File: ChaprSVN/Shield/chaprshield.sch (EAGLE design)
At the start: 2 parts

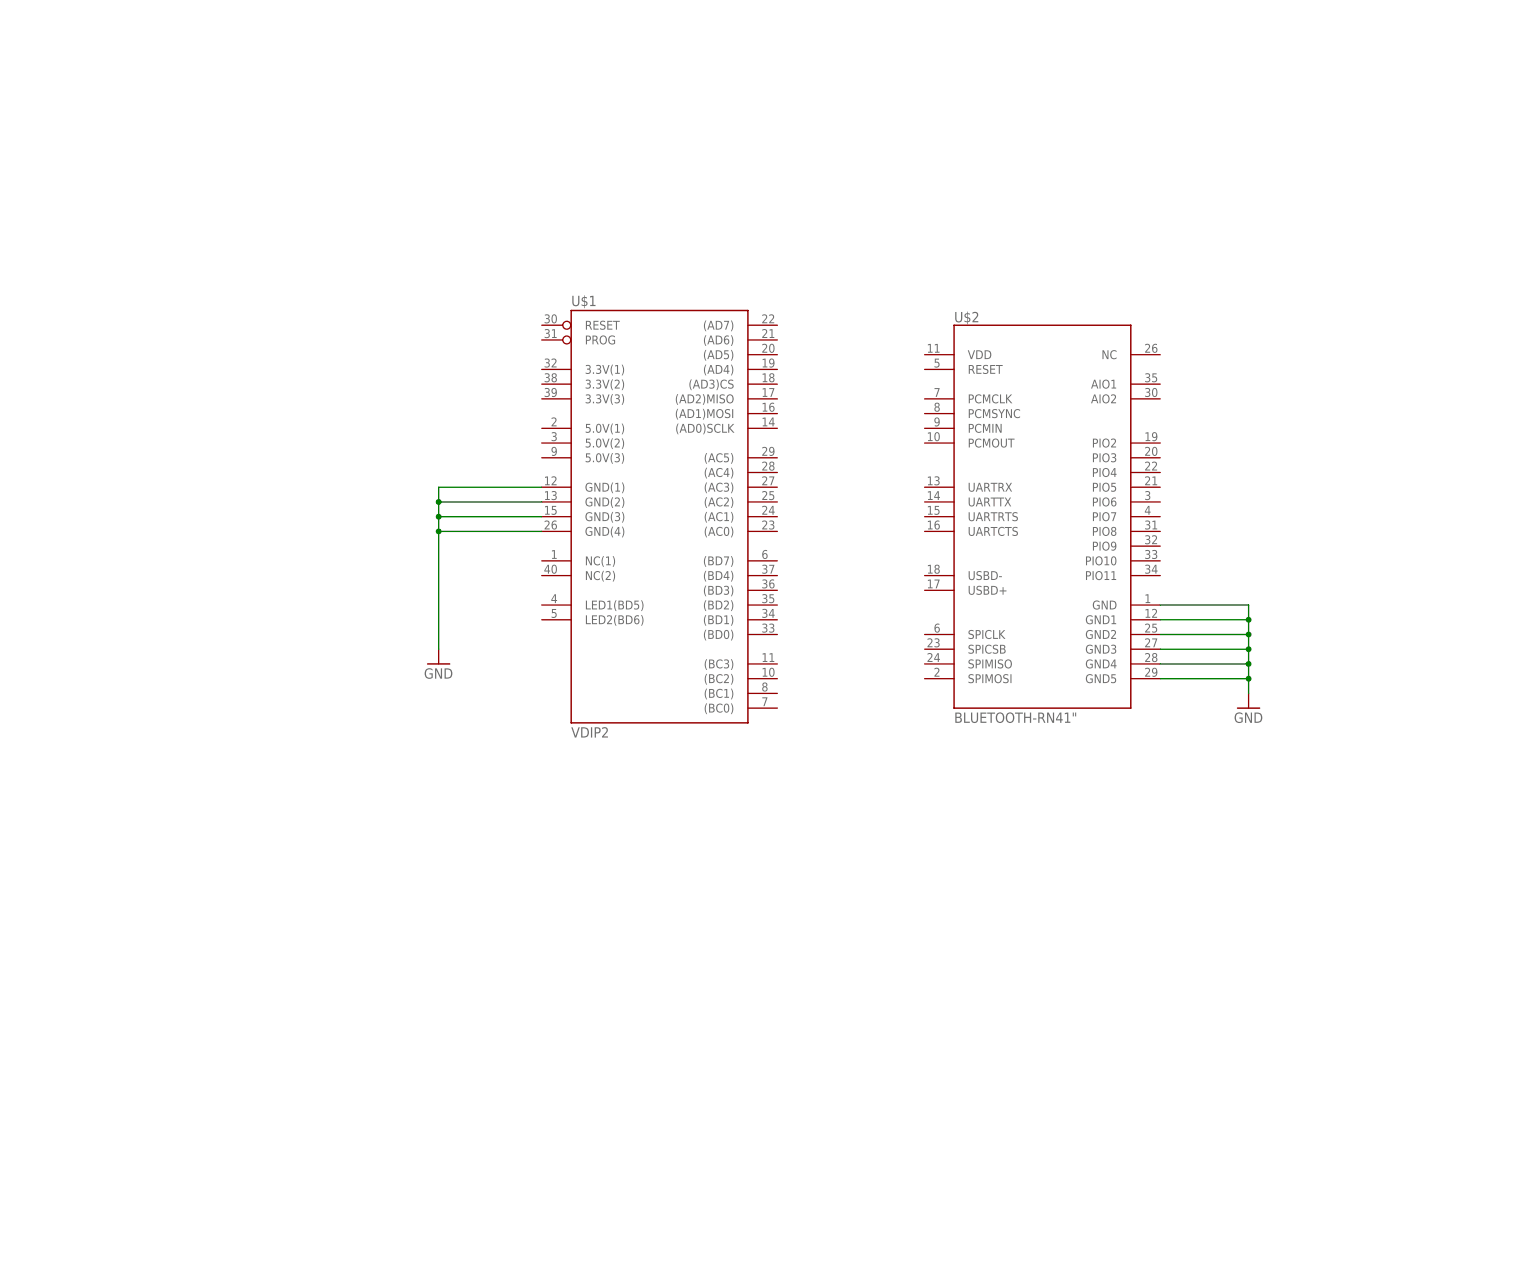
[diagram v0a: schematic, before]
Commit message: Added pin headers and started wiring.
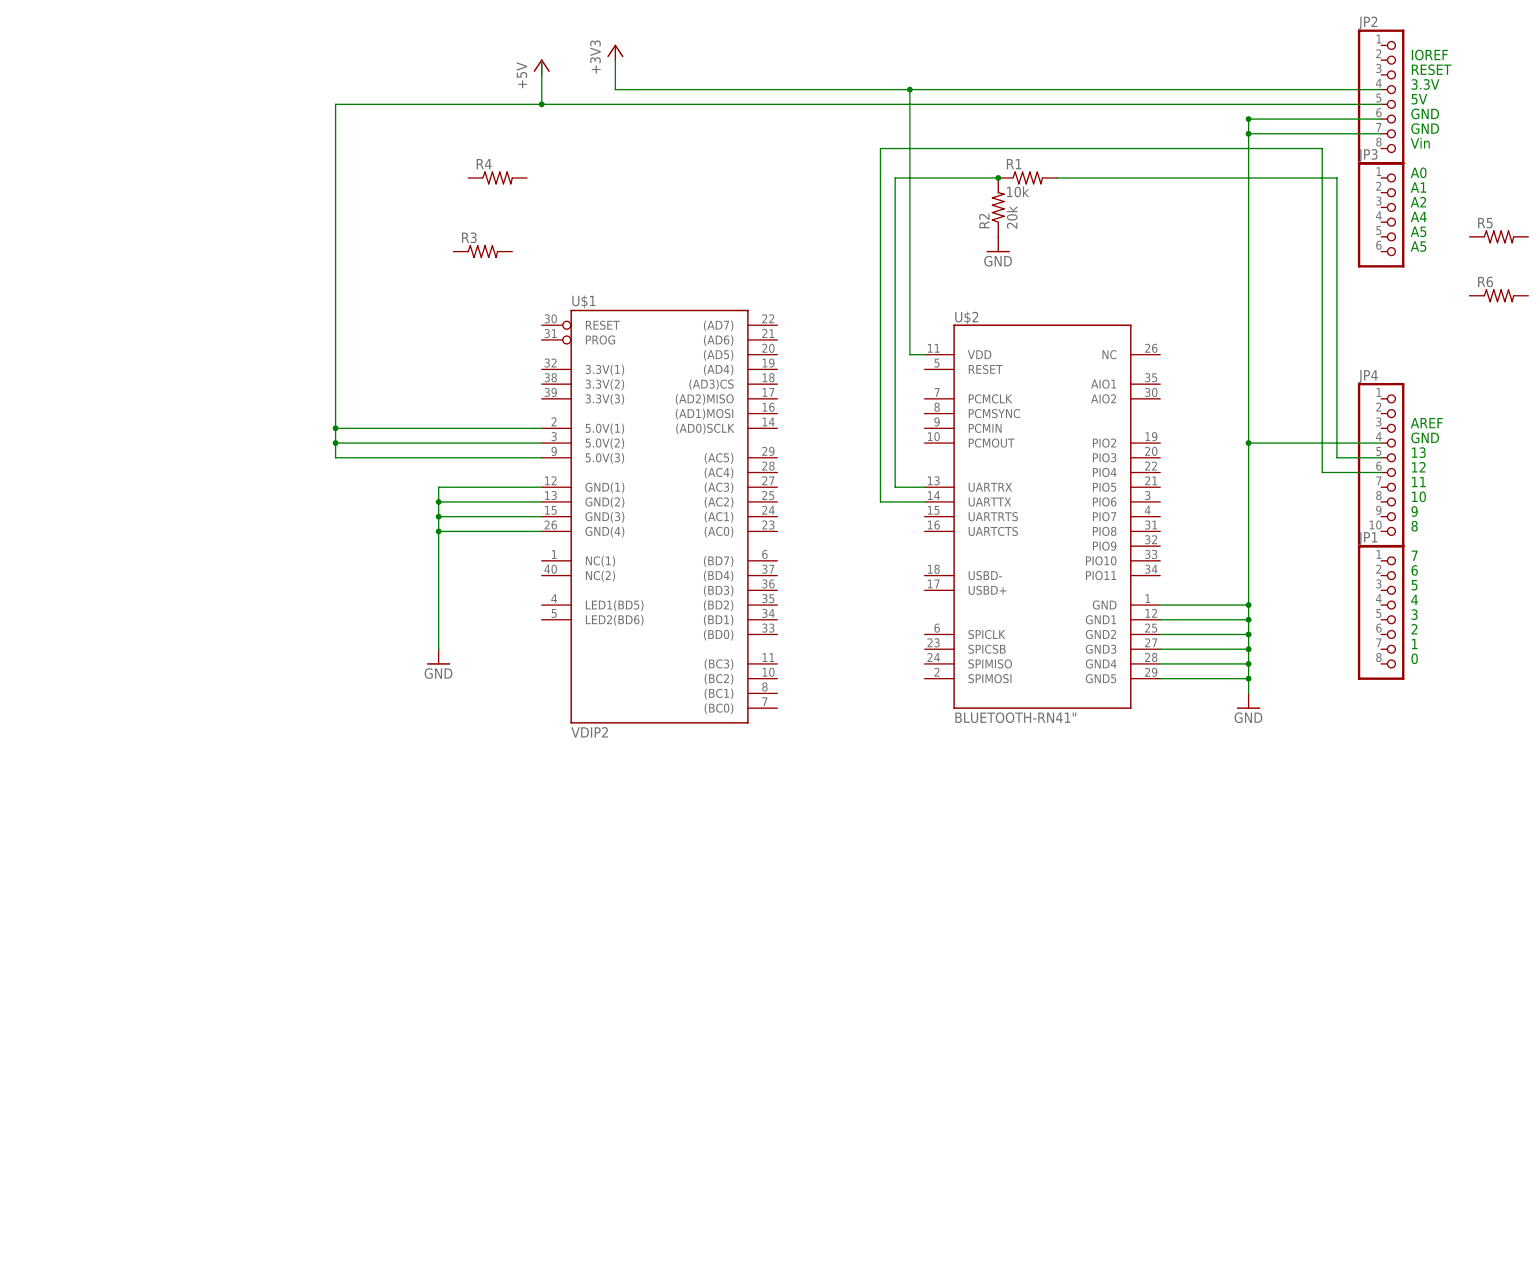
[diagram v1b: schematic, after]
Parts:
- added JP1, JP2: (no value), pinhead:PINHD-1X8
- added JP3: (no value), pinhead:PINHD-1X6
- added JP4: (no value), pinhead:PINHD-1X10
- added R1: 10k, resistor:R-US_0207/10
- added R2: 20k, resistor:R-US_0207/10
- added R3, R4, R5, R6: (no value), resistor:R-US_0207/10
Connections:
- new net N$1: JP2.5, U$1.5.0V(1), U$1.5.0V(2), U$1.5.0V(3)
- new net N$2: JP2.4, U$2.VDD
- new net N$3: JP4.5, R1.2
- new net N$4: R1.1, R2.2, U$2.UARTRX
- new net N$5: JP4.6, U$2.UARTTX
- net GND: now also JP2.6, JP2.7, JP4.4, R2.1
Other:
- note added: "0"
- note added: "1"
- note added: "10"
- note added: "11"
- note added: "12"
- note added: "13"
- note added: "2"
- note added: "3"
- note added: "3.3V"
- note added: "4"
- note added: "5"
- note added: "5V"
- note added: "6"
- note added: "7"
- note added: "8"
- note added: "9"
- note added: "A0"
- note added: "A1"
- note added: "A2"
- note added: "A4"
- note added: "A5"
- note added: "AREF"
- note added: "GND"
- note added: "IOREF"
- note added: "RESET"
- note added: "Vin"
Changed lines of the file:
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@@
 <part name="U$2" library="SparkFun-RF" deviceset="BLUETOOTH-RN41" device="&quot;"/>
 <part name="GND2" library="supply1" deviceset="GND" device=""/>
+<part name="JP1" library="pinhead" deviceset="PINHD-1X8" device=""/>
+<part name="JP2" library="pinhead" deviceset="PINHD-1X8" device=""/>
+<part name="JP3" library="pinhead" deviceset="PINHD-1X6" device=""/>
+<part name="JP4" library="pinhead" deviceset="PINHD-1X10" device=""/>
+<part name="+3V1" library="supply1" deviceset="+3V3" device=""/>
+<part name="P+1" library="supply1" deviceset="+5V" device=""/>
+<part name="R1" library="resistor" deviceset="R-US_" device="0207/10" value="10k"/>
+<part name="R2" library="resistor" deviceset="R-US_" device="0207/10" value="20k"/>
+<part name="R3" library="resistor" deviceset="R-US_" device="0207/10"/>
+<part name="R4" library="resistor" deviceset="R-US_" device="0207/10"/>
+<part name="R5" library="resistor" deviceset="R-US_" device="0207/10"/>
+<part name="R6" library="resistor" deviceset="R-US_" device="0207/10"/>
+<part name="GND3" library="supply1" deviceset="GND" device=""/>
 </parts>
 <sheets>
 <sheet>
 <plain>
+<text x="154.94" y="60.96" size="1.778" layer="91">13</text>
+<text x="154.94" y="58.42" size="1.778" layer="91">12</text>
+<text x="154.94" y="55.88" size="1.778" layer="91">11</text>
+<text x="154.94" y="53.34" size="1.778" layer="91">10</text>
+<text x="154.94" y="50.8" size="1.778" layer="91">9</text>
+<text x="154.94" y="48.26" size="1.778" layer="91">8</text>
+<text x="154.94" y="43.18" size="1.778" layer="91">7</text>
+<text x="154.94" y="40.64" size="1.778" layer="91">6</text>
+<text x="154.94" y="38.1" size="1.778" layer="91">5</text>
+<text x="154.94" y="35.56" size="1.778" layer="91">4</text>
+<text x="154.94" y="33.02" size="1.778" layer="91">3</text>
+<text x="154.94" y="30.48" size="1.778" layer="91">2</text>
+<text x="154.94" y="27.94" size="1.778" layer="91">1</text>
+<text x="154.94" y="25.4" size="1.778" layer="91">0</text>
+<text x="154.94" y="63.5" size="1.778" layer="91">GND</text>
+<text x="154.94" y="116.84" size="1.778" layer="91">GND</text>
+<text x="154.94" y="119.38" size="1.778" layer="91">GND</text>
+<text x="154.94" y="96.52" size="1.778" layer="91">A5</text>
+<text x="154.94" y="99.06" size="1.778" layer="91">A5</text>
+<text x="154.94" y="101.6" size="1.778" layer="91">A4</text>
+<text x="154.94" y="104.14" size="1.778" layer="91">A2</text>
+<text x="154.94" y="106.68" size="1.778" layer="91">A1</text>
+<text x="154.94" y="109.22" size="1.778" layer="91">A0</text>
+<text x="154.94" y="114.3" size="1.778" layer="91">Vin</text>
+<text x="154.94" y="121.92" size="1.778" layer="91">5V</text>
+<text x="154.94" y="124.46" size="1.778" layer="91">3.3V</text>
+<text x="154.94" y="127" size="1.778" layer="91">RESET</text>
+<text x="154.94" y="129.54" size="1.778" layer="91">IOREF</text>
+<text x="154.94" y="66.04" size="1.778" layer="91">AREF</text>
 </plain>
 <instances>
@@
 <instance part="U$2" gate="G$1" x="91.44" y="50.8"/>
 <instance part="GND2" gate="1" x="127" y="17.78"/>
+<instance part="JP1" gate="A" x="152.4" y="33.02"/>
+<instance part="JP2" gate="A" x="152.4" y="121.92"/>
+<instance part="JP3" gate="A" x="152.4" y="101.6"/>
+<instance part="JP4" gate="A" x="152.4" y="60.96"/>
+<instance part="+3V1" gate="G$1" x="17.78" y="132.08"/>
+<instance part="P+1" gate="1" x="5.08" y="129.54"/>
+<instance part="R1" gate="G$1" x="88.9" y="109.22"/>
+<instance part="R2" gate="G$1" x="83.82" y="104.14" rot="R90"/>
+<instance part="R3" gate="G$1" x="-5.08" y="96.52"/>
+<instance part="R4" gate="G$1" x="-2.54" y="109.22"/>
+<instance part="R5" gate="G$1" x="170.18" y="99.06"/>
+<instance part="R6" gate="G$1" x="170.18" y="88.9"/>
+<instance part="GND3" gate="1" x="83.82" y="96.52"/>
 </instances>
 <busses>
@@
 <junction x="127" y="25.4"/>
 <junction x="127" y="22.86"/>
+<wire x1="127" y1="63.5" x2="127" y2="35.56" width="0.1524" layer="91"/>
+<junction x="127" y="35.56"/>
+<pinref part="JP4" gate="A" pin="4"/>
+<wire x1="149.86" y1="63.5" x2="127" y2="63.5" width="0.1524" layer="91"/>
+<pinref part="JP2" gate="A" pin="6"/>
+<wire x1="149.86" y1="119.38" x2="127" y2="119.38" width="0.1524" layer="91"/>
+<wire x1="127" y1="119.38" x2="127" y2="116.84" width="0.1524" layer="91"/>
+<pinref part="JP2" gate="A" pin="7"/>
+<wire x1="127" y1="116.84" x2="127" y2="63.5" width="0.1524" layer="91"/>
+<wire x1="149.86" y1="116.84" x2="127" y2="116.84" width="0.1524" layer="91"/>
+<junction x="127" y="119.38"/>
+<junction x="127" y="116.84"/>
+<junction x="127" y="63.5"/>
+</segment>
+<segment>
+<pinref part="R2" gate="G$1" pin="1"/>
+<pinref part="GND3" gate="1" pin="GND"/>
 </segment>
 </net>
+<net name="N$1" class="0">
+<segment>
+<pinref part="JP2" gate="A" pin="5"/>
+<wire x1="149.86" y1="121.92" x2="5.08" y2="121.92" width="0.1524" layer="91"/>
+<wire x1="5.08" y1="121.92" x2="5.08" y2="129.54" width="0.1524" layer="91"/>
+<pinref part="U$1" gate="G$1" pin="5.0V(3)"/>
+<wire x1="5.08" y1="60.96" x2="-30.48" y2="60.96" width="0.1524" layer="91"/>
+<wire x1="-30.48" y1="60.96" x2="-30.48" y2="63.5" width="0.1524" layer="91"/>
+<wire x1="-30.48" y1="63.5" x2="-30.48" y2="66.04" width="0.1524" layer="91"/>
+<wire x1="-30.48" y1="66.04" x2="-30.48" y2="121.92" width="0.1524" layer="91"/>
+<wire x1="-30.48" y1="121.92" x2="5.08" y2="121.92" width="0.1524" layer="91"/>
+<junction x="5.08" y="121.92"/>
+<pinref part="U$1" gate="G$1" pin="5.0V(2)"/>
+<wire x1="5.08" y1="63.5" x2="-30.48" y2="63.5" width="0.1524" layer="91"/>
+<pinref part="U$1" gate="G$1" pin="5.0V(1)"/>
+<wire x1="5.08" y1="66.04" x2="-30.48" y2="66.04" width="0.1524" layer="91"/>
+<junction x="-30.48" y="66.04"/>
+<junction x="-30.48" y="63.5"/>
+</segment>
+</net>
+<net name="N$2" class="0">
+<segment>
+<pinref part="JP2" gate="A" pin="4"/>
+<wire x1="149.86" y1="124.46" x2="68.58" y2="124.46" width="0.1524" layer="91"/>
+<wire x1="68.58" y1="124.46" x2="17.78" y2="124.46" width="0.1524" layer="91"/>
+<wire x1="17.78" y1="124.46" x2="17.78" y2="129.54" width="0.1524" layer="91"/>
+<pinref part="U$2" gate="G$1" pin="VDD"/>
+<wire x1="71.12" y1="78.74" x2="68.58" y2="78.74" width="0.1524" layer="91"/>
+<wire x1="68.58" y1="78.74" x2="68.58" y2="124.46" width="0.1524" layer="91"/>
+<junction x="68.58" y="124.46"/>
+</segment>
+</net>
+<net name="N$3" class="0">
+<segment>
+<pinref part="R1" gate="G$1" pin="2"/>
+<wire x1="93.98" y1="109.22" x2="142.24" y2="109.22" width="0.1524" layer="91"/>
+<wire x1="142.24" y1="109.22" x2="142.24" y2="60.96" width="0.1524" layer="91"/>
+<pinref part="JP4" gate="A" pin="5"/>
+<wire x1="149.86" y1="60.96" x2="142.24" y2="60.96" width="0.1524" layer="91"/>
+</segment>
+</net>
+<net name="N$4" class="0">
+<segment>
+<pinref part="R1" gate="G$1" pin="1"/>
+<pinref part="R2" gate="G$1" pin="2"/>
+<wire x1="83.82" y1="109.22" x2="66.04" y2="109.22" width="0.1524" layer="91"/>
+<wire x1="66.04" y1="109.22" x2="66.04" y2="55.88" width="0.1524" layer="91"/>
+<pinref part="U$2" gate="G$1" pin="UARTRX"/>
+<wire x1="66.04" y1="55.88" x2="71.12" y2="55.88" width="0.1524" layer="91"/>
+<junction x="83.82" y="109.22"/>
+</segment>
+</net>
+<net name="N$5" class="0">
+<segment>
+<pinref part="U$2" gate="G$1" pin="UARTTX"/>
+<wire x1="71.12" y1="53.34" x2="63.5" y2="53.34" width="0.1524" layer="91"/>
+<wire x1="63.5" y1="53.34" x2="63.5" y2="114.3" width="0.1524" layer="91"/>
+<wire x1="63.5" y1="114.3" x2="139.7" y2="114.3" width="0.1524" layer="91"/>
+<wire x1="139.7" y1="114.3" x2="139.7" y2="58.42" width="0.1524" layer="91"/>
+<pinref part="JP4" gate="A" pin="6"/>
+<wire x1="139.7" y1="58.42" x2="149.86" y2="58.42" width="0.1524" layer="91"/>
+</segment>
+</net>
